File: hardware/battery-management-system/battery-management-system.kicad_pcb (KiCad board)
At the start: 4 copper layers, 100 x 100 mm, 152 parts, among them IC1 LT8584EFE#PBF, J1 CELLS, J10 TEMP_CELL3, J11 TEMP_CELL4, J2 Charge, J3 Discharge, J4 VBAT_DISCHARGE, J6 AMPHENOL_micro_usb_10118194-0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, J7 ARM-JTAG-SWD, J8 TEMP_CELL1, J9 TEMP_CELL2, Q1 DMN3404L, Q10 DMN3404L, Q11 BS250FTA, Q12 BS250FTA, Q13 BS250FTA, Q14 BS250FTA, Q15 BS250FTA, Q2 TJ40S04M3L, Q3 TJ40S04M3L, Q4 DMN3404L, Q6 DMN3404L, Q7 DMN3404L, Q8 DMN3404L, Q9 DMN3404L, T1 NA6252-ALD, U1 ICL7660, U10 LM2904M8-13, U11 STC3100, U2 L6982CDR, U3 L6982CDR, U4 ICL7660, U5 FT230XS, U6 AT24C512C, U7 NCT75DR2G, U8 STM32L071CZTx, U9 LM2904M8-13

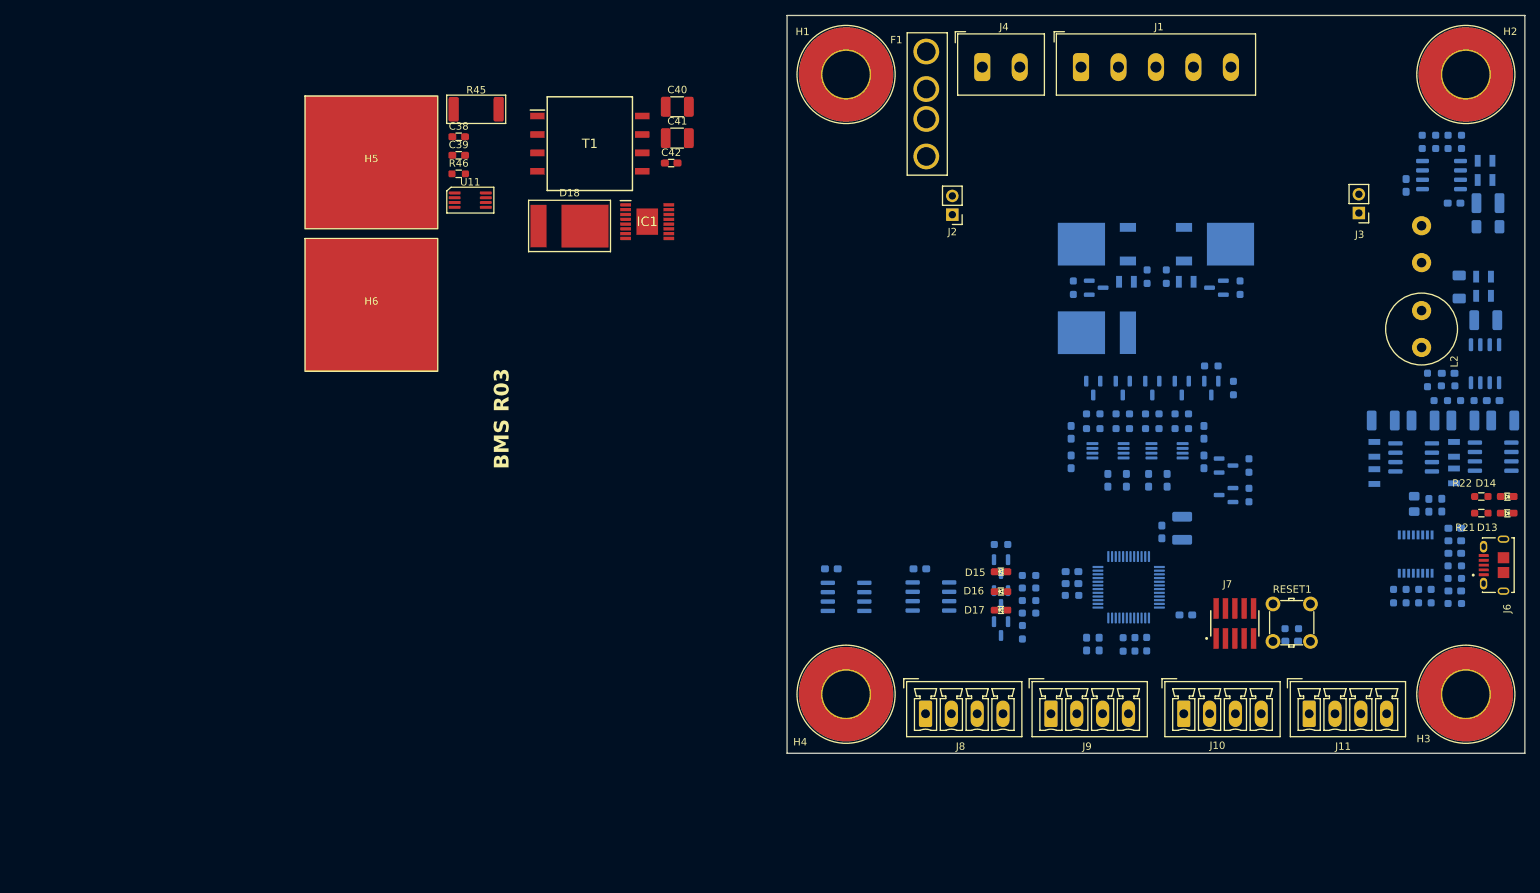
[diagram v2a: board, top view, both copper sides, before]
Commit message: update PCB from schematic
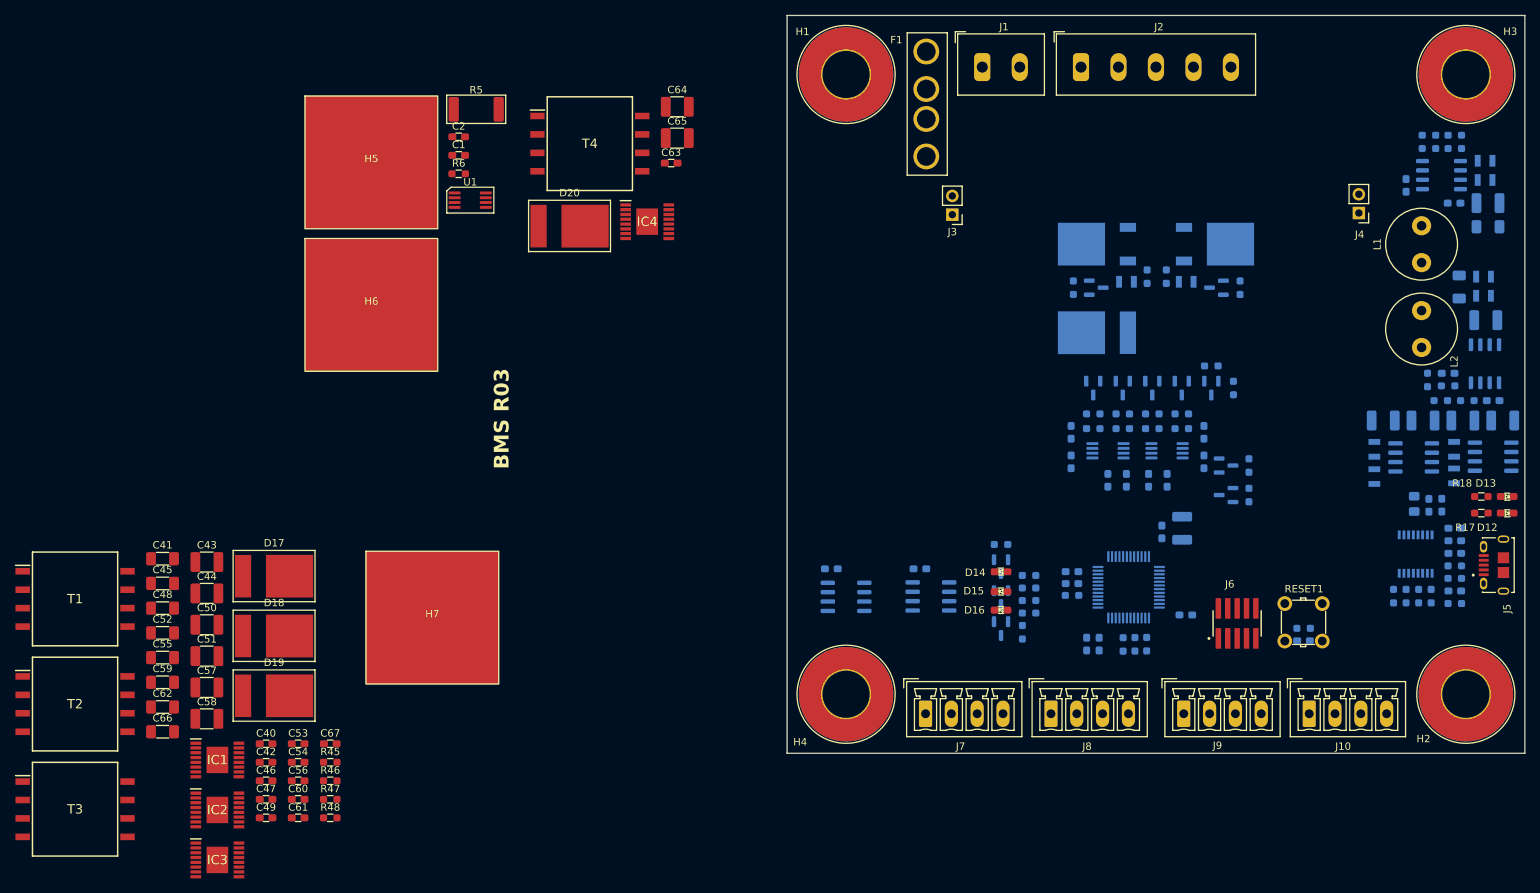
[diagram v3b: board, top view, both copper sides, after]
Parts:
- added C40: 22nF, benediktibk:C_0603_1608Metric_Pad1.08x0.95mm_HandSolder, F.Cu at (-50.6, 118.7)
- added C41: 47uF, benediktibk:C_1206_3216Metric_Pad1.33x1.80mm_HandSolder, F.Cu at (-64.6, 93.6)
- added C42: 1uF, benediktibk:C_0603_1608Metric_Pad1.08x0.95mm_HandSolder, F.Cu at (-50.6, 121.2)
- added C43: 10uF, benediktibk:C_1210_3225Metric_Pad1.33x2.70mm_HandSolder, F.Cu at (-58.6, 94.1)
- added C44: 10uF, benediktibk:C_1210_3225Metric_Pad1.33x2.70mm_HandSolder, F.Cu at (-58.6, 98.3)
- added C45: 47uF, benediktibk:C_1206_3216Metric_Pad1.33x1.80mm_HandSolder, F.Cu at (-64.6, 97.0)
- added C46: 47nF, benediktibk:C_0603_1608Metric_Pad1.08x0.95mm_HandSolder, F.Cu at (-50.6, 123.7)
- added C47: 22nF, benediktibk:C_0603_1608Metric_Pad1.08x0.95mm_HandSolder, F.Cu at (-50.6, 126.2)
- added C48: 47uF, benediktibk:C_1206_3216Metric_Pad1.33x1.80mm_HandSolder, F.Cu at (-64.6, 100.3)
- added C49: 1uF, benediktibk:C_0603_1608Metric_Pad1.08x0.95mm_HandSolder, F.Cu at (-50.6, 128.8)
- added C50: 10uF, benediktibk:C_1210_3225Metric_Pad1.33x2.70mm_HandSolder, F.Cu at (-58.6, 102.6)
- added C51: 10uF, benediktibk:C_1210_3225Metric_Pad1.33x2.70mm_HandSolder, F.Cu at (-58.6, 106.8)
- added C52: 47uF, benediktibk:C_1206_3216Metric_Pad1.33x1.80mm_HandSolder, F.Cu at (-64.6, 103.7)
- added C53: 47nF, benediktibk:C_0603_1608Metric_Pad1.08x0.95mm_HandSolder, F.Cu at (-46.3, 118.7)
- added C54: 22nF, benediktibk:C_0603_1608Metric_Pad1.08x0.95mm_HandSolder, F.Cu at (-46.3, 121.2)
- added C55: 47uF, benediktibk:C_1206_3216Metric_Pad1.33x1.80mm_HandSolder, F.Cu at (-64.6, 107.0)
- added C56: 1uF, benediktibk:C_0603_1608Metric_Pad1.08x0.95mm_HandSolder, F.Cu at (-46.3, 123.7)
- added C57: 10uF, benediktibk:C_1210_3225Metric_Pad1.33x2.70mm_HandSolder, F.Cu at (-58.6, 111.1)
- added C58: 10uF, benediktibk:C_1210_3225Metric_Pad1.33x2.70mm_HandSolder, F.Cu at (-58.6, 115.3)
- added C59: 47uF, benediktibk:C_1206_3216Metric_Pad1.33x1.80mm_HandSolder, F.Cu at (-64.6, 110.4)
- added C60: 47nF, benediktibk:C_0603_1608Metric_Pad1.08x0.95mm_HandSolder, F.Cu at (-46.3, 126.2)
- added C61: 22nF, benediktibk:C_0603_1608Metric_Pad1.08x0.95mm_HandSolder, F.Cu at (-46.3, 128.8)
- added C62: 47uF, benediktibk:C_1206_3216Metric_Pad1.33x1.80mm_HandSolder, F.Cu at (-64.6, 113.7)
- added C66: 47uF, benediktibk:C_1206_3216Metric_Pad1.33x1.80mm_HandSolder, F.Cu at (-64.6, 117.1)
- added C67: 47nF, benediktibk:C_0603_1608Metric_Pad1.08x0.95mm_HandSolder, F.Cu at (-41.9, 118.7)
- added D17: SBR2065D1, benediktibk:SBR2065D1, F.Cu at (-49.5, 96.0)
- added D18: SBR2065D1, benediktibk:SBR2065D1, F.Cu at (-49.5, 104.1)
- added D19: SBR2065D1, benediktibk:SBR2065D1, F.Cu at (-49.5, 112.2)
- added H7: heatsink_18x18, benediktibk:heatsink_18x18, F.Cu at (-28.1, 101.6)
- added IC1: LT8584EFE#PBF, benediktibk:SOP65P640X110-17N, F.Cu at (-57.2, 120.9)
- added IC2: LT8584EFE#PBF, benediktibk:SOP65P640X110-17N, F.Cu at (-57.2, 127.7)
- added IC3: LT8584EFE#PBF, benediktibk:SOP65P640X110-17N, F.Cu at (-57.2, 134.5)
- added R45: 4.7kOhm, benediktibk:R_0603_1608Metric_Pad0.98x0.95mm_HandSolder, F.Cu at (-41.9, 121.2)
- added R46: 4.7kOhm, benediktibk:R_0603_1608Metric_Pad0.98x0.95mm_HandSolder, F.Cu at (-41.9, 123.7)
- added R47: 4.7kOhm, benediktibk:R_0603_1608Metric_Pad0.98x0.95mm_HandSolder, F.Cu at (-41.9, 126.2)
- added R48: 4.7kOhm, benediktibk:R_0603_1608Metric_Pad0.98x0.95mm_HandSolder, F.Cu at (-41.9, 128.8)
- added T1: NA6252-ALD, benediktibk:SOP250P1524X1143-8N, F.Cu at (-76.5, 99.1)
- added T2: NA6252-ALD, benediktibk:SOP250P1524X1143-8N, F.Cu at (-76.5, 113.3)
- added T3: NA6252-ALD, benediktibk:SOP250P1524X1143-8N, F.Cu at (-76.5, 127.6)
- L1: moved to F.Cu
- moved R24 1.60 mm to (90.0, 103.1)
- moved C29 1.60 mm to (90.0, 104.8)
- moved RESET1 1.60 mm to (90.0, 102.2)
- moved J6 0.31 mm to (81.0, 102.4)
- renumbered C39 to C1, C6 to C10, C1 to C11, C4 to C12, C9 to C13, C10 to C14, C18 to C15, C13 to C16, C15 to C17, C17 to C18, C14 to C19, C38 to C2, C16 to C20, C19 to C21, C21 to C22, C22 to C23, C27 to C26, C28 to C27, C29 to C28, C26 to C29, C8 to C3, C20 to C30, C23 to C31, C30 to C32, C31 to C33, C32 to C34, C33 to C35, C34 to C36, C35 to C37, C36 to C38, C37 to C39, C11 to C4, C2 to C5, C5 to C6, C42 to C63, C40 to C64, C41 to C65, C12 to C8, C3 to C9, D9 to D10, D10 to D11, D13 to D12, D14 to D13, D15 to D14, D16 to D15, D17 to D16, D18 to D20, D6 to D4, D7 to D5, D11 to D6, D12 to D7, D5 to D8, D8 to D9, H3 to H2, H2 to H3, IC1 to IC4, J4 to J1, J11 to J10, J1 to J2, J2 to J3, J3 to J4, J6 to J5, J7 to J6, J8 to J7, J9 to J8, J10 to J9, Q2 to Q1, Q12 to Q10, Q13 to Q11, Q14 to Q12, Q15 to Q13, Q9 to Q14, Q3 to Q2, Q1 to Q3, Q6 to Q5, Q7 to Q6, Q8 to Q7, Q11 to Q8, Q10 to Q9, R2 to R1, R21 to R17, R22 to R18, R17 to R19, R4 to R2, R18 to R20, R19 to R21, R20 to R22, R32 to R23, R27 to R24, R30 to R25, R31 to R26, R24 to R27, R26 to R28, R1 to R3, R23 to R30, R25 to R31, R28 to R32, R36 to R33, R37 to R35, R39 to R36, R35 to R37, R41 to R38, R43 to R39, R3 to R4, R33 to R40, R38 to R41, R40 to R42, R42 to R43, R45 to R5, R46 to R6, T1 to T4, U11 to U1, U9 to U10, U10 to U11, U1 to U4, U4 to U5, U5 to U6, U8 to U7, U6 to U8, U7 to U9
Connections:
- C63 pad 1: /Cell Balancing/PACK -> /Battery Pack/PACK
- C63 pad 2: /Cell Balancing/CELL1_MINUS -> Net-(C63-Pad2)
- C64 pad 1: /Cell Balancing/PACK -> /Battery Pack/PACK
- C64 pad 2: /Cell Balancing/CELL1_MINUS -> Net-(C63-Pad2)
- C65 pad 1: /Cell Balancing/PACK -> /Battery Pack/PACK
- C65 pad 2: /Cell Balancing/CELL1_MINUS -> Net-(C63-Pad2)
- D20 pad 1: Net-(D18-A) -> Net-(D20-A)
- D20 pad 2: /Cell Balancing/PACK -> /Battery Pack/PACK
- IC4 pad 1: unconnected-(IC1-GND_1-Pad1) -> /Battery Pack/CELL1_MINUS
- IC4 pad 10: unconnected-(IC1-VCELL-Pad10) -> /Battery Pack/CELL2_MINUS
- IC4 pad 11: unconnected-(IC1-VSNS-Pad11) -> /Battery Pack/CELL2_MINUS
- IC4 pad 12: unconnected-(IC1-DCHRG-Pad12) -> /Battery Pack/CELL2_MINUS
- IC4 pad 13: unconnected-(IC1-SW_1-Pad13) -> /Battery Pack/CELL2_MINUS
- IC4 pad 14: unconnected-(IC1-SW_2-Pad14) -> /Battery Pack/CELL2_MINUS
- IC4 pad 15: unconnected-(IC1-SW_3-Pad15) -> /Battery Pack/CELL2_MINUS
- IC4 pad 16: unconnected-(IC1-SW_4-Pad16) -> /Battery Pack/CELL2_MINUS
- IC4 pad 17: GND -> /Battery Pack/CELL1_MINUS
- IC4 pad 2: unconnected-(IC1-GND_2-Pad2) -> /Battery Pack/CELL1_MINUS
- IC4 pad 3: unconnected-(IC1-GND_3-Pad3) -> /Battery Pack/CELL1_MINUS
- IC4 pad 4: unconnected-(IC1-GND_4-Pad4) -> /Battery Pack/CELL1_MINUS
- IC4 pad 5: unconnected-(IC1-MODE-Pad5) -> /Battery Pack/CELL2_MINUS
- IC4 pad 6: unconnected-(IC1-RTMR-Pad6) -> GND
- IC4 pad 7: unconnected-(IC1-DIN-Pad7) -> /Cell Balancing/CELL1_ENABLE
- IC4 pad 8: unconnected-(IC1-OUT-Pad8) -> Net-(IC4-OUT)
- IC4 pad 9: unconnected-(IC1-VIN-Pad9) -> /Battery Pack/CELL2_MINUS
- T4 pad 1: /Cell Balancing/CELL1_MINUS -> /Battery Pack/CELL2_MINUS
- T4 pad 2: /Cell Balancing/CELL1_MINUS -> /Battery Pack/CELL2_MINUS
- T4 pad 3: Net-(D18-A) -> /Battery Pack/CELL2_MINUS
- T4 pad 4: Net-(D18-A) -> /Battery Pack/CELL2_MINUS
- T4 pad 5: unconnected-(T1-Pad5) -> Net-(C63-Pad2)
- T4 pad 8: unconnected-(T1-Pad8) -> Net-(D20-A)
- U1 pad 3: /Battery Pack/SDA -> /MCU/SDA
- U1 pad 4: /Battery Pack/SCL -> /MCU/SCL
- U7 pad 14: unconnected-(U8-PA4-Pad14) -> /Cell Balancing/CELL1_ENABLE
- U7 pad 15: unconnected-(U8-PA5-Pad15) -> /Cell Balancing/CELL2_ENABLE
- U7 pad 16: unconnected-(U8-PA6-Pad16) -> /Cell Balancing/CELL3_ENABLE
- U7 pad 17: unconnected-(U8-PA7-Pad17) -> /Cell Balancing/CELL4_ENABLE
- U7 pad 28: /MCU/CHARGE_AVAILABLE -> unconnected-(U7-PB15-Pad28)

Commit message: finish placement of BMS R03
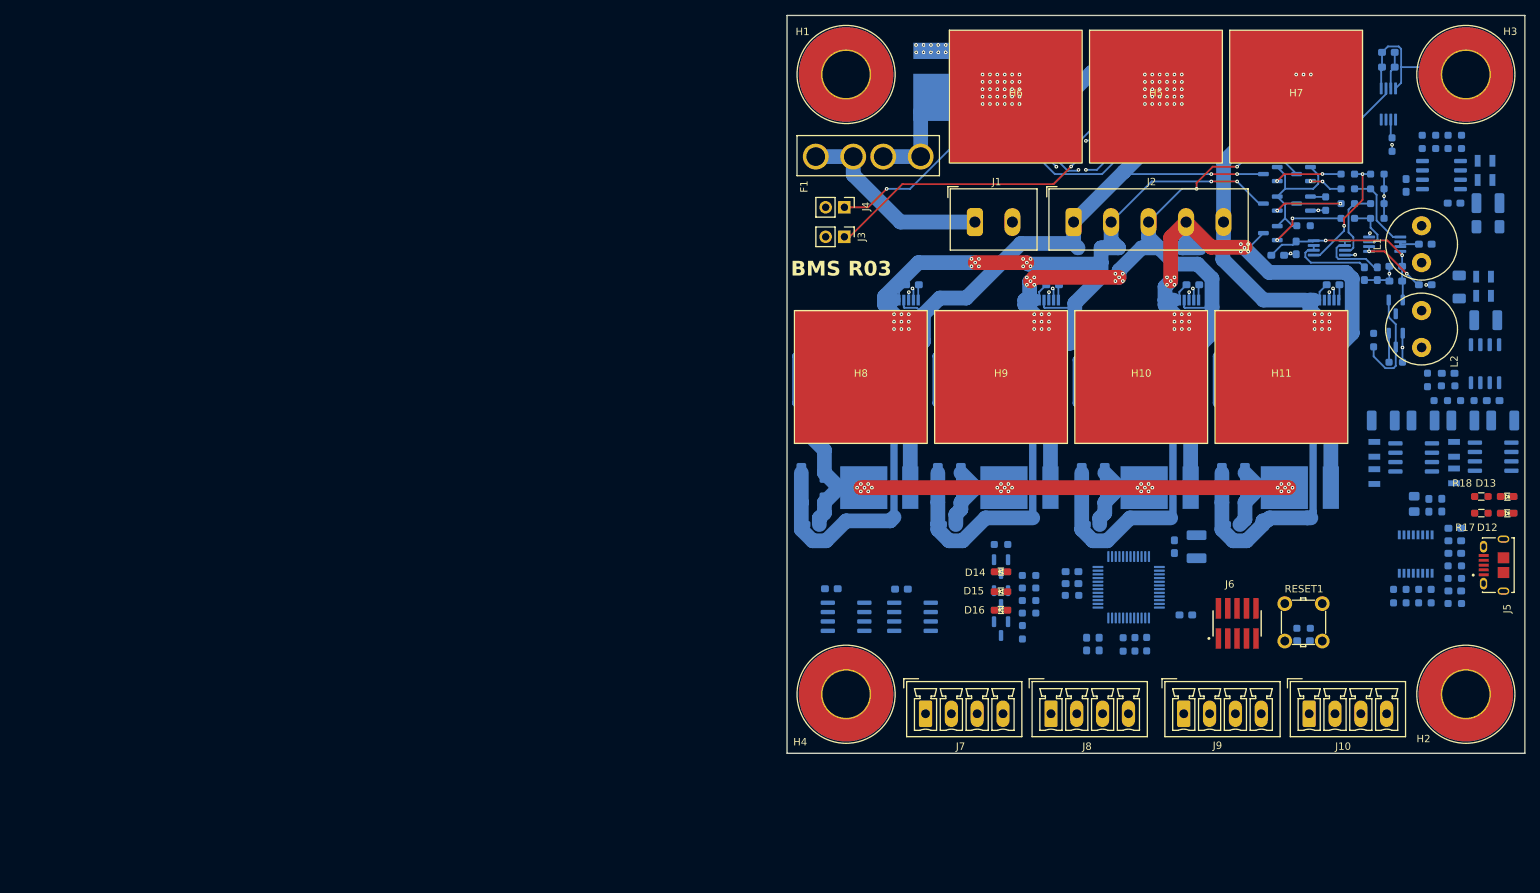
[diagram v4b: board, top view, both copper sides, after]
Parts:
- added H10: heatsink_18x18, benediktibk:heatsink_18x18, F.Cu at (68.0, 69.0)
- added H11: heatsink_18x18, benediktibk:heatsink_18x18, F.Cu at (87.0, 69.0)
- added H8: heatsink_18x18, benediktibk:heatsink_18x18, F.Cu at (30.0, 69.0)
- added H9: heatsink_18x18, benediktibk:heatsink_18x18, F.Cu at (49.0, 69.0)
- C1, C2, C40, C41, C42, C43, C44, C45, C46, C47, C48, C49, C50, C51, C52, C53, C54, C55, C56, C57, C58, C59, C60, C61, C62, C63, C64, C65, C66, C67, D17, D18, D19, D20, IC1, IC2, IC3, IC4, R45, R46, R47, R48, R5, R6, T1, T2, T3, T4, U1: moved to B.Cu
- moved C62 160.4 mm to (87.5, 63.0), turned to 90 degrees
- moved C66 156.5 mm to (77.5, 51.5)
- moved T3 154.5 mm to (68.0, 73.0)
- moved IC3 149.7 mm to (73.5, 61.5), turned to -90 degrees
- moved C67 149.5 mm to (94.0, 56.5), turned to 180 degrees
- moved C59 148.8 mm to (72.0, 51.5)
- moved C61 141.5 mm to (79.5, 64.0), turned to 90 degrees
- moved C52 141.1 mm to (66.5, 51.5)
- moved R48 140.7 mm to (82.5, 63.0)
- moved C55 140.2 mm to (68.5, 63.0), turned to 90 degrees
- moved C60 139.9 mm to (75.0, 56.5), turned to 180 degrees
- moved H7 136.7 mm to (89.0, 31.0)
- moved C45 133.6 mm to (61.0, 51.5)
- moved T2 131.8 mm to (49.0, 73.0)
- moved IC2 129.8 mm to (54.5, 61.5), turned to -90 degrees
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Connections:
- IC1 pad 13: /Battery Pack/PACK -> Net-(IC1-SW_1)
- IC1 pad 14: /Battery Pack/PACK -> Net-(IC1-SW_1)
- IC1 pad 15: /Battery Pack/PACK -> Net-(IC1-SW_1)
- IC1 pad 16: /Battery Pack/PACK -> Net-(IC1-SW_1)
- IC2 pad 13: /Battery Pack/CELL4_MINUS -> Net-(IC2-SW_1)
- IC2 pad 14: /Battery Pack/CELL4_MINUS -> Net-(IC2-SW_1)
- IC2 pad 15: /Battery Pack/CELL4_MINUS -> Net-(IC2-SW_1)
- IC2 pad 16: /Battery Pack/CELL4_MINUS -> Net-(IC2-SW_1)
- IC3 pad 13: /Battery Pack/CELL3_MINUS -> Net-(IC3-SW_1)
- IC3 pad 14: /Battery Pack/CELL3_MINUS -> Net-(IC3-SW_1)
- IC3 pad 15: /Battery Pack/CELL3_MINUS -> Net-(IC3-SW_1)
- IC3 pad 16: /Battery Pack/CELL3_MINUS -> Net-(IC3-SW_1)
- IC4 pad 13: /Battery Pack/CELL2_MINUS -> Net-(IC4-SW_1)
- IC4 pad 14: /Battery Pack/CELL2_MINUS -> Net-(IC4-SW_1)
- IC4 pad 15: /Battery Pack/CELL2_MINUS -> Net-(IC4-SW_1)
- IC4 pad 16: /Battery Pack/CELL2_MINUS -> Net-(IC4-SW_1)
- R45 pad 2: /Battery Pack/PACK -> Net-(IC1-SW_1)
- R46 pad 2: /Battery Pack/CELL4_MINUS -> Net-(IC2-SW_1)
- R47 pad 2: /Battery Pack/CELL3_MINUS -> Net-(IC3-SW_1)
- R48 pad 2: /Battery Pack/CELL2_MINUS -> Net-(IC4-SW_1)
- T1 pad 3: /Battery Pack/PACK -> Net-(IC1-SW_1)
- T1 pad 4: /Battery Pack/PACK -> Net-(IC1-SW_1)
- T2 pad 3: /Battery Pack/CELL4_MINUS -> Net-(IC2-SW_1)
- T2 pad 4: /Battery Pack/CELL4_MINUS -> Net-(IC2-SW_1)
- T3 pad 3: /Battery Pack/CELL3_MINUS -> Net-(IC3-SW_1)
- T3 pad 4: /Battery Pack/CELL3_MINUS -> Net-(IC3-SW_1)
- T4 pad 3: /Battery Pack/CELL2_MINUS -> Net-(IC4-SW_1)
- T4 pad 4: /Battery Pack/CELL2_MINUS -> Net-(IC4-SW_1)
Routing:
- net /Battery Pack/PACK: track 0.00 -> 237.3 mm, vias 0 -> 60
- net /Battery Pack/CELL4_MINUS: track 0.00 -> 133.0 mm, vias 0 -> 21
- net /Battery Pack/CELL3_MINUS: track 0.00 -> 123.5 mm, vias 0 -> 21
- net /Battery Pack/CELL2_MINUS: track 0.00 -> 106.1 mm, vias 0 -> 19
- net /5V_USB: track 85.1 -> 0.00 mm
- net /Battery Pack/CELL1_MINUS: track 0.00 -> 64.9 mm, vias 0 -> 9
- net GND: track 0.00 -> 51.4 mm, vias 0 -> 28
- net Net-(J3-Pin_1): track 0.00 -> 48.1 mm, vias 0 -> 1
- net /5V: track 47.6 -> 0.00 mm
- net Net-(C63-Pad2): track 0.00 -> 42.3 mm
- net Net-(C42-Pad2): track 0.00 -> 42.0 mm
- net Net-(C49-Pad2): track 0.00 -> 42.0 mm
- net Net-(C56-Pad2): track 0.00 -> 41.8 mm
- net Net-(J4-Pin_1): track 0.00 -> 41.0 mm, vias 0 -> 1
- net Net-(J1-Pin_1): track 0.00 -> 26.7 mm
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
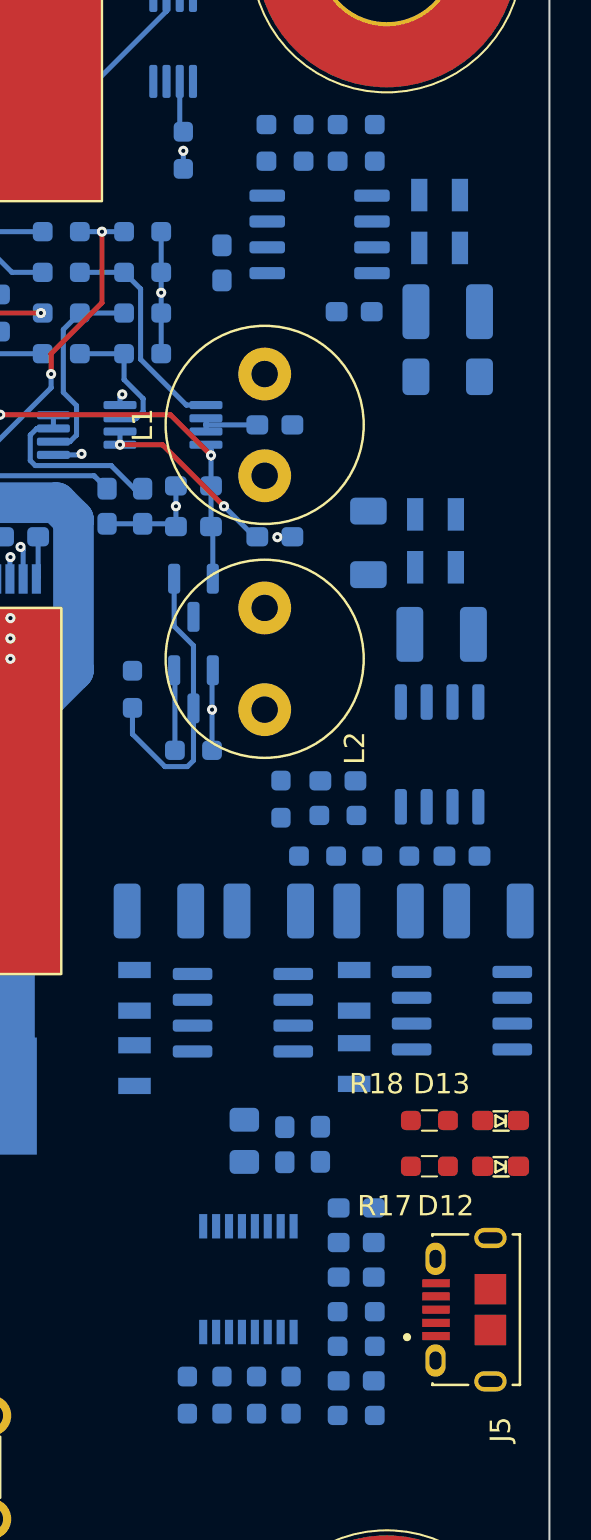
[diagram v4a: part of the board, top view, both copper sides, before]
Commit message: improve layout of BMS
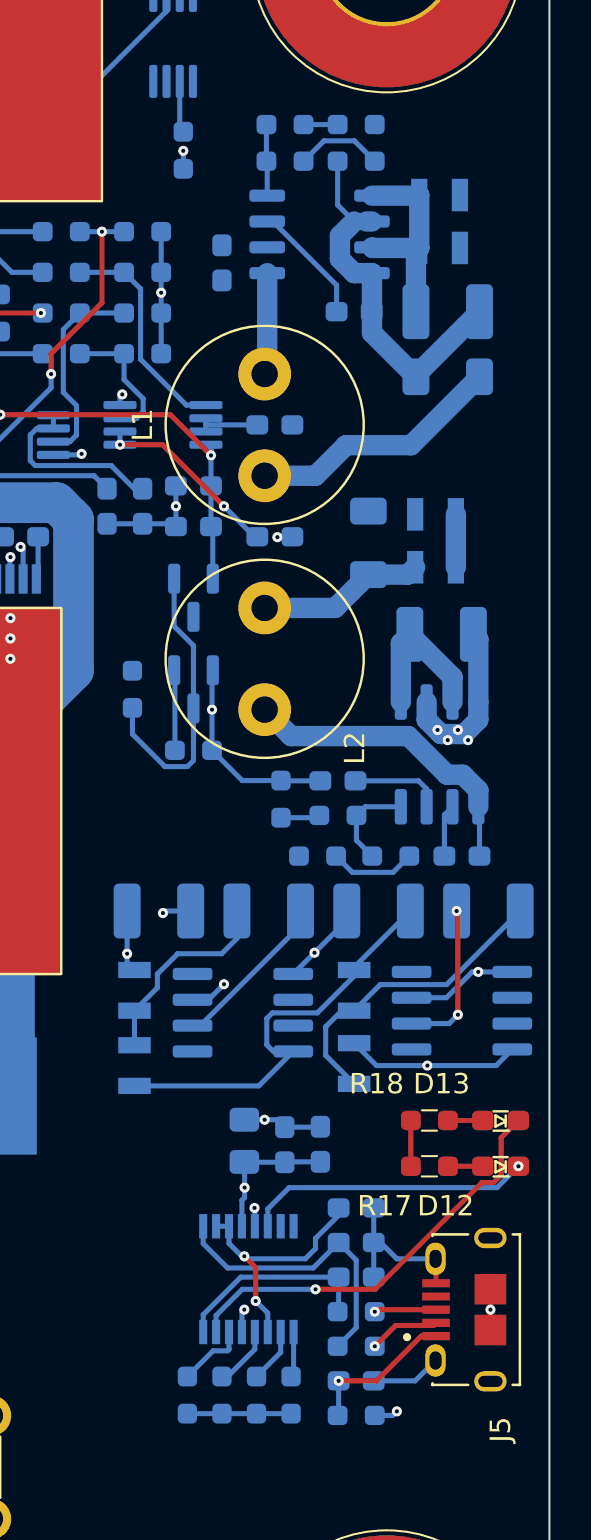
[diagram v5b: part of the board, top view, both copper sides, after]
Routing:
- net GND: track 51.4 -> 116.6 mm, vias 28 -> 40
- net /Power Supply/9V4: track 0.00 -> 20.7 mm
- net Net-(D13-K): track 0.00 -> 20.7 mm, vias 0 -> 1
- net /3V3: track 5.11 -> 22.8 mm
- net Net-(U3-SW): track 0.00 -> 15.4 mm
- net Net-(D8-K): track 0.00 -> 15.3 mm
- net Net-(U6-USBDM): track 0.00 -> 14.4 mm
- net Net-(D12-K): track 0.00 -> 14.0 mm, vias 0 -> 1
- net Net-(U6-3V3OUT): track 0.00 -> 12.9 mm, vias 0 -> 2
- net /5V: track 0.00 -> 11.2 mm, vias 0 -> 1
- net Net-(D4-K): track 0.00 -> 10.5 mm
- net /5V_USB: track 0.00 -> 10.4 mm, vias 0 -> 2
- net Net-(U6-USBDP): track 0.00 -> 10.00 mm
- net Net-(D10-K): track 0.00 -> 9.95 mm
- net Net-(D6-A): track 0.00 -> 8.23 mm
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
